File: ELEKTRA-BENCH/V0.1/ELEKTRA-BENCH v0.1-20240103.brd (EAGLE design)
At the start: 40 x 27 mm, 37 parts, among them U2 LMR14030, U3 MP1601GTF-Z

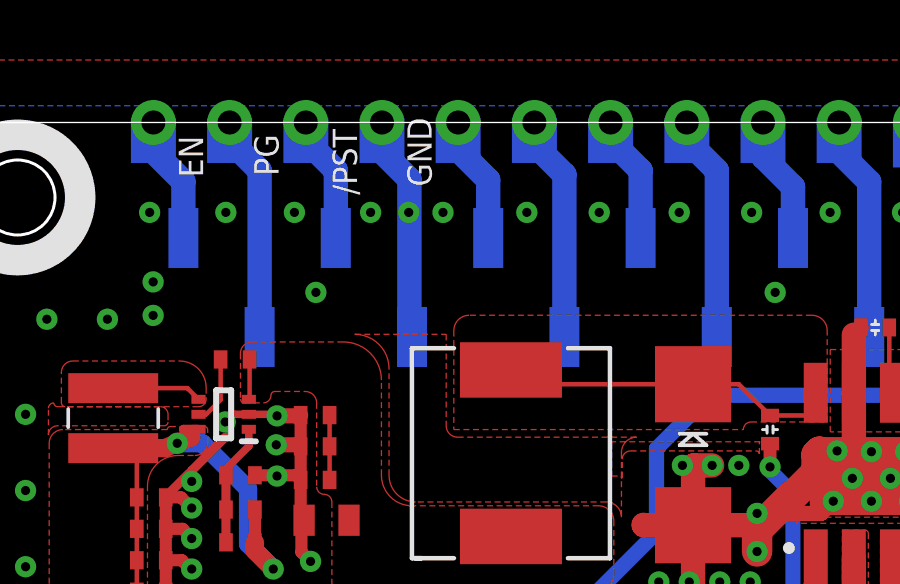
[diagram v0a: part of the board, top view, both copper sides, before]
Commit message: Design elektra PMIC and Bench modules
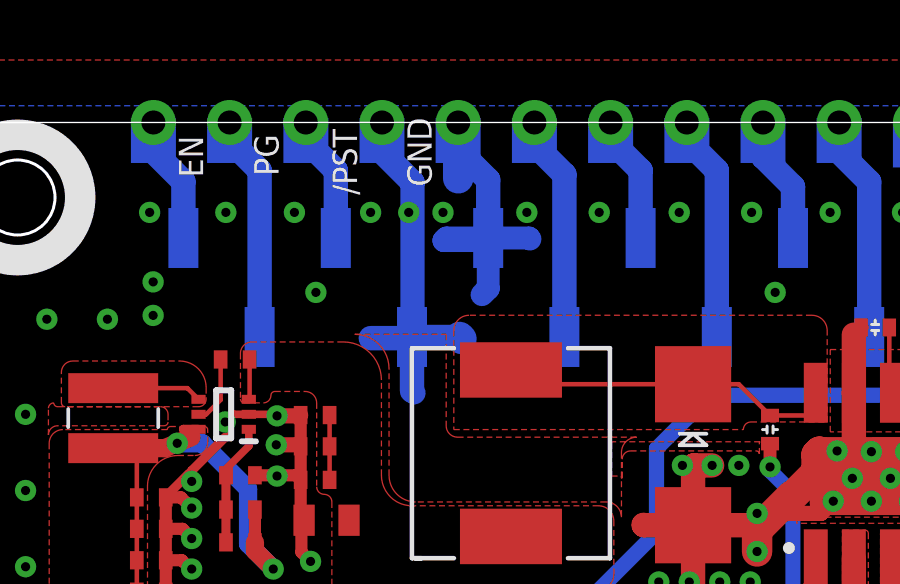
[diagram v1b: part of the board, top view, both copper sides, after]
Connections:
- removed net N$1: CONN1.8, U$4.8, U$4.P$8
- net GND: now also CONN1.8, U$4.8, U$4.P$8
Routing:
- net GND: track 119.6 -> 136.5 mm
- net N$1: track 4.26 -> 0.00 mm
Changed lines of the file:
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@@
 <drawing>
 <settings>
-<setting alwaysvectorfont="yes"/>
+<setting alwaysvectorfont="no"/>
 <setting verticaltext="up"/>
 </settings>
@@
 <contactref element="U$3" pad="P$9"/>
 <contactref element="U$3" pad="9"/>
-<wire x1="15.5644" y1="25.1046" x2="14.65" y2="26.019" width="0.8128" layer="16"/>
+<wire x1="15.666" y1="25.003" x2="14.65" y2="26.019" width="0.8128" layer="16"/>
 <wire x1="14.65" y1="26.4" x2="14.65" y2="26.019" width="0.8128" layer="16"/>
-<wire x1="15.5644" y1="25.1046" x2="15.5644" y2="20.4356" width="0.8128" layer="16"/>
-<wire x1="15.5644" y1="20.4356" x2="15.65" y2="19.85" width="0.8128" layer="16"/>
+<wire x1="15.65" y1="19.85" x2="15.666" y2="19.866" width="0.8128" layer="16"/>
+<wire x1="15.666" y1="25.003" x2="15.666" y2="19.866" width="0.8128" layer="16"/>
 <wire x1="24.81" y1="1.6764" x2="24.35" y2="2.1364" width="0.8128" layer="16"/>
 <wire x1="24.35" y1="2.1364" x2="24.35" y2="7.15" width="0.8128" layer="16"/>
@@
 <wire x1="27.35" y1="0.6" x2="27.35" y2="1.6002" width="0.8128" layer="16"/>
 <wire x1="30.3784" y1="17.9896" x2="30.3784" y2="19.9264" width="0.8128" layer="1"/>
+<contactref element="CONN1" pad="8"/>
+<contactref element="U$4" pad="8"/>
+<contactref element="U$4" pad="P$8"/>
+<wire x1="18.19" y1="25.0856" x2="17.19" y2="26.0856" width="0.8128" layer="16"/>
+<wire x1="17.19" y1="27" x2="17.19" y2="26.4" width="0.8128" layer="16"/>
+<wire x1="18.19" y1="25.0856" x2="18.19" y2="23.15" width="0.8128" layer="16"/>
+<wire x1="17.19" y1="26.4" x2="17.19" y2="26.0856" width="0.8128" layer="16"/>
+<wire x1="17.19" y1="26.4" x2="17.19" y2="25.1402" width="1.016" layer="16"/>
+<wire x1="15.65" y1="19.85" x2="15.612" y2="19.812" width="1.016" layer="16"/>
+<wire x1="15.612" y1="19.812" x2="14.2748" y2="19.812" width="0.8128" layer="16"/>
+<wire x1="15.65" y1="19.85" x2="17.234" y2="19.85" width="0.8128" layer="16"/>
+<wire x1="17.234" y1="19.85" x2="17.2974" y2="19.7866" width="1.016" layer="16"/>
+<wire x1="15.65" y1="19.85" x2="15.65" y2="18.0558" width="0.8128" layer="16"/>
+<wire x1="15.65" y1="18.0558" x2="15.7226" y2="17.9832" width="0.762" layer="16"/>
+<wire x1="18.19" y1="23.15" x2="18.19" y2="21.4666" width="0.762" layer="16"/>
+<wire x1="18.19" y1="21.4666" x2="17.9832" y2="21.2598" width="0.762" layer="16"/>
+<wire x1="18.19" y1="23.15" x2="18.1032" y2="23.0632" width="0.762" layer="16"/>
+<wire x1="18.1032" y1="23.0632" x2="16.7132" y2="23.0632" width="0.762" layer="16"/>
+<wire x1="16.7132" y1="23.0632" x2="16.8" y2="23.15" width="0.762" layer="16"/>
+<wire x1="16.8" y1="23.15" x2="18.19" y2="23.15" width="0.762" layer="16"/>
+<wire x1="18.19" y1="23.15" x2="19.5474" y2="23.15" width="0.762" layer="16"/>
+<wire x1="19.5474" y1="23.15" x2="19.5834" y2="23.114" width="0.762" layer="16"/>
 </signal>
 <signal name="+3V3">
@@
 <wire x1="35.8014" y1="15.72006875" x2="35.78900625" y2="15.71" width="0.1524" layer="1"/>
 </signal>
-<signal name="N$1">
-<contactref element="CONN1" pad="8"/>
-<contactref element="U$4" pad="8"/>
-<contactref element="U$4" pad="P$8"/>
-<wire x1="18.19" y1="25.0856" x2="17.19" y2="26.0856" width="0.8128" layer="16"/>
-<wire x1="17.19" y1="27" x2="17.19" y2="26.4" width="0.8128" layer="16"/>
-<wire x1="18.19" y1="25.0856" x2="18.19" y2="23.15" width="0.8128" layer="16"/>
-<wire x1="17.19" y1="26.4" x2="17.19" y2="26.0856" width="0.8128" layer="16"/>
-</signal>
 <signal name="N$3">

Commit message: upload PCB and sch
upload PCB and sch
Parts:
- R2: value 39.2K -> 12K
- R3: value 30K -> 82K
- R4: value 47K -> 82K
